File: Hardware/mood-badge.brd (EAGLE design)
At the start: 76.2 x 101.6 mm, 90 parts

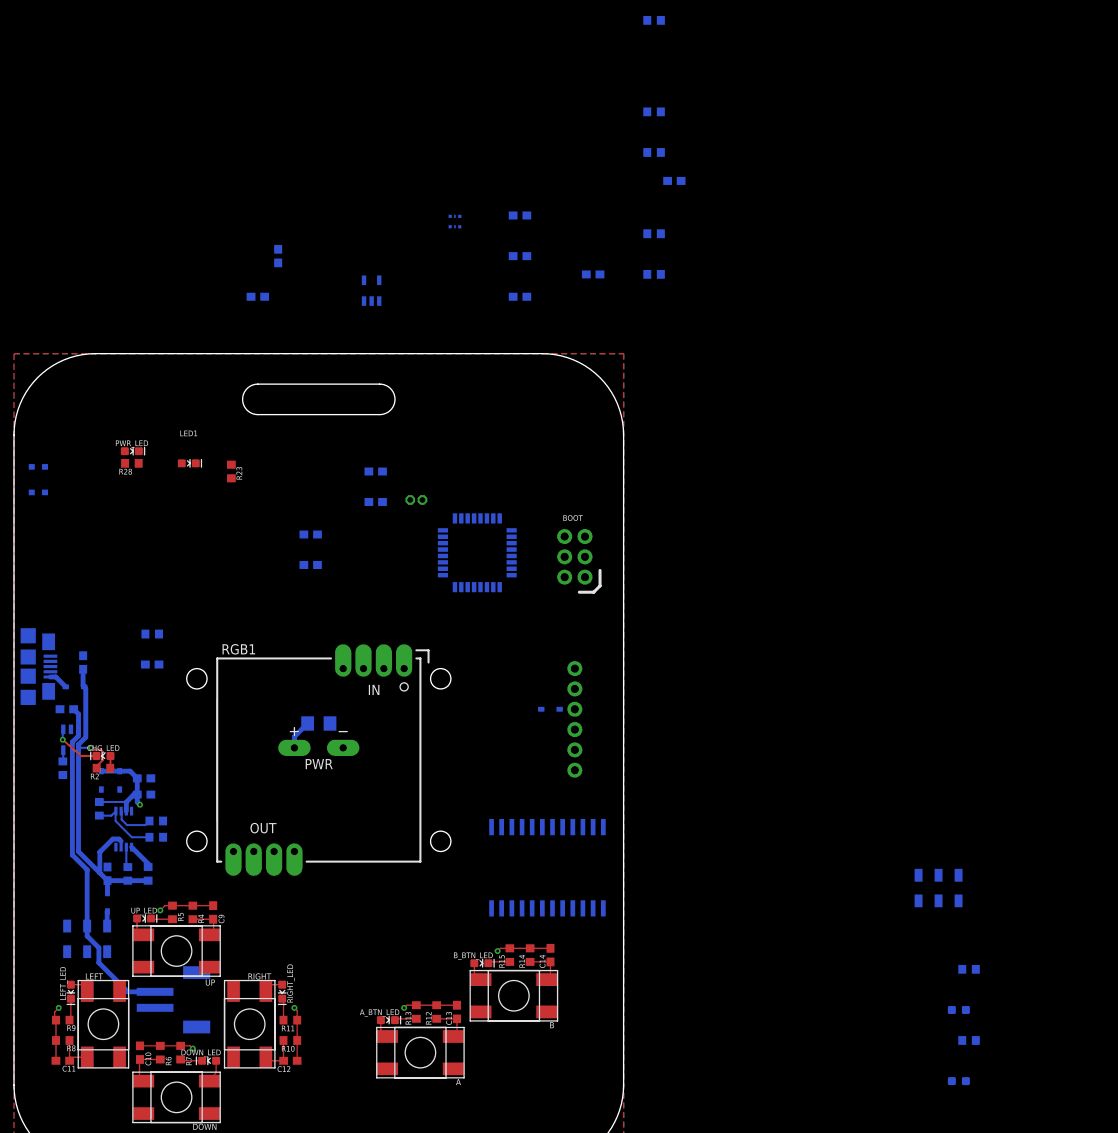
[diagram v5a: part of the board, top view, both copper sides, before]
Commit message: Adjustments to PCB trace widths and connections to buttons added
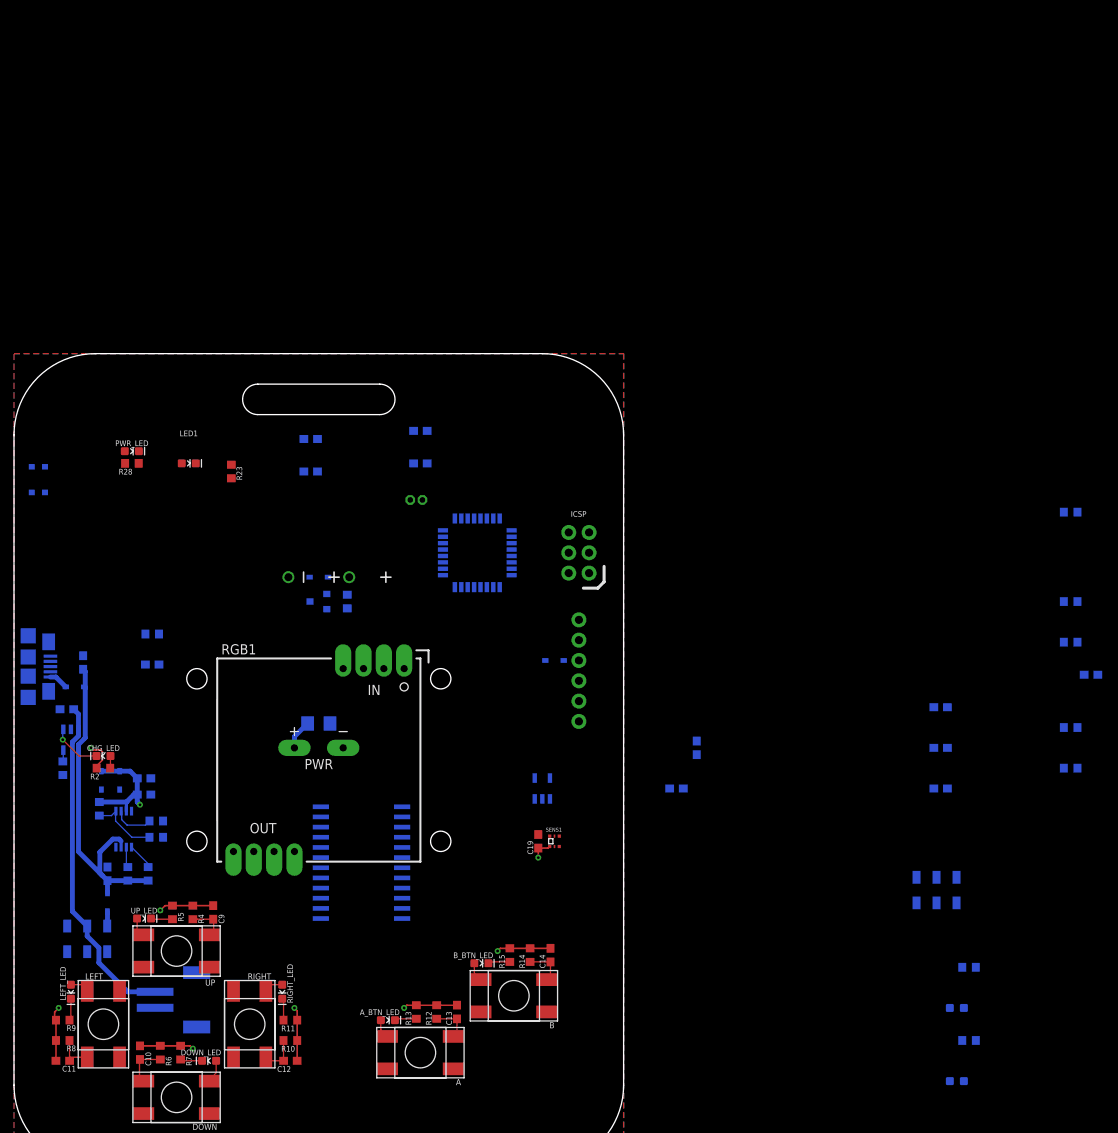
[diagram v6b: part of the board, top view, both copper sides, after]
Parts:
- removed BOOT: AVR_SPI_PROG_3X2NS, LinnesLab-Connectors:2X3-NS
- added D6: (no value), LinnesLab-DiscreteSemi:USC
- added ICSP: AVR_SPI_PROG_3X2NS, LinnesLab-Connectors:2X3-NS
- added LS1: CVS-1508, SparkFun-Electromechanical:CVS-1508_PCBSPKR
- added Q1: (no value), LinnesLab-DiscreteSemi:SOT23-3
- added R29: 180, LinnesLab-Passives:R0603
- moved C15 80.9 mm to (115.8, 57.4)
- moved C16 80.9 mm to (115.8, 52.3)
- moved C17 80.9 mm to (115.8, 47.2)
- moved R21 80.8 mm to (132.1, 54.9)
- moved R22 80.8 mm to (132.1, 49.8)
- moved C18 80.8 mm to (134.6, 61.5)
- moved C20 80.7 mm to (82.8, 47.2)
- moved C21 80.7 mm to (85.3, 52.3)
- moved R18 80.6 mm to (132.1, 81.8)
- moved R19 80.4 mm to (132.1, 70.6)
- moved R20 80.4 mm to (132.1, 65.5)
- moved SENS1 78.5 mm to (67.6, 40.6), flipped to the top
- moved C19 71.2 mm to (65.5, 40.6), flipped to the top, turned to 90 degrees
- moved OP1 65.8 mm to (66.0, 47.2)
- moved I/O 23.9 mm to (43.4, 37.3), turned to 90 degrees
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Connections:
- removed net ACTION: ARDUINO.19
- removed net LD1: ARDUINO.2
- removed net LD12: ARDUINO.14
- removed net LD13: ARDUINO.13
- removed net LD14: ARDUINO.12
- removed net LD15: ARDUINO.11
- removed net LD16: ARDUINO.10
- removed net LD2: ARDUINO.1
- removed net LD3: ARDUINO.32
- removed net LD6: ARDUINO.26
- removed net LD7: ARDUINO.25
- removed net LD8: ARDUINO.24
- removed net N$10: C10.1, DOWN.3, DOWN.4, DOWN_LED.A, R6.1
- removed net N$12: C11.1, LEFT.3, LEFT.4, LEFT_LED.A, R8.1
- removed net N$14: C12.1, R10.1, RIGHT.3, RIGHT.4, RIGHT_LED.A
- removed net N$16: A.3, A.4, A_BTN_LED.A, C13.1, R12.1
- removed net N$18: B.3, B.4, B_BTN_LED.A, C14.1, R14.1
- removed net N$8: C9.1, R4.1, UP.3, UP.4, UP_LED.A
- new net A_BTN: A.3, A.4, ARDUINO.1, A_BTN_LED.A, C13.1, R12.1
- new net B_BTN: ARDUINO.2, B.3, B.4, B_BTN_LED.A, C14.1, R14.1
- new net DOWN: ARDUINO.14, C10.1, DOWN.3, DOWN.4, DOWN_LED.A, R6.1
- new net N$31: Q1.1, R29.2
- new net N$5: D6.+, LS1.-, Q1.3
- new net SPKR: ARDUINO.12, R29.1
- new net UP: ARDUINO.13, C9.1, R4.1, UP.3, UP.4, UP_LED.A
- net GND: now also ICSP.6, Q1.2; no longer BOOT.6
- net LEFT: now also ARDUINO.11, C11.1, LEFT.3, LEFT.4, LEFT_LED.A, R8.1; no longer ARDUINO.23
- net MISO: now also ICSP.1; no longer BOOT.1
- net MOSI: now also ICSP.4; no longer BOOT.4
- net PULSE: now also ARDUINO.32
- net RESET: now also ICSP.5; no longer BOOT.5
- net RIGHT: now also ARDUINO.10, C12.1, R10.1, RIGHT.3, RIGHT.4, RIGHT_LED.A; no longer ARDUINO.22
- net SCK: now also ICSP.3; no longer BOOT.3
- net VCC: now also D6.-, ICSP.2, LS1.+; no longer BOOT.2
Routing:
- net N$10: track 10.8 -> 0.00 mm
- net DOWN: track 0.00 -> 10.8 mm
- net N$12: track 8.34 -> 0.00 mm
- net LEFT: track 0.00 -> 8.34 mm
- net UP: track 0.00 -> 7.92 mm
- net N$8: track 7.92 -> 0.00 mm
- net RIGHT: track 0.00 -> 7.51 mm
- net N$14: track 7.51 -> 0.00 mm
- net N$16: track 7.32 -> 0.00 mm
- net A_BTN: track 0.00 -> 7.32 mm
- net N$18: track 7.32 -> 0.00 mm
- net B_BTN: track 0.00 -> 7.32 mm
- net GND: track 41.6 -> 44.4 mm, vias 6 -> 7
- net VIN: track 47.2 -> 46.2 mm
- net V_USB: track 2.43 -> 3.10 mm

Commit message: PCB Routed
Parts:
- removed CHG_LED, PWR_LED: (no value), LinnesLab-LED:LED-0603
- removed I/O: PCF8575C, SparkFun-Retired:SO-24DW
- added CHG, PWR: (no value), LinnesLab-LED:LED-0603
- moved MODE_2 86.1 mm to (61.5, 75.7), flipped to the top, turned to 180 degrees
- moved R17 84.8 mm to (61.5, 77.7), flipped to the top
- moved MODE_1 83.8 mm to (61.5, 81.8), flipped to the top
- moved R16 79.8 mm to (61.5, 79.8), flipped to the top, turned to 180 degrees
- moved R19 70.7 mm to (62.5, 58.4), turned to 270 degrees
- moved R21 69.6 mm to (62.5, 53.8), turned to 90 degrees
- moved R18 69.4 mm to (68.6, 53.8), turned to 90 degrees
- moved R22 68.2 mm to (64.0, 53.8), turned to 270 degrees
- moved C18 67.0 mm to (68.6, 50.3), turned to 90 degrees
- moved R20 66.2 mm to (68.6, 46.7), turned to 90 degrees
- moved MODE 66.2 mm to (66.0, 78.7), flipped to the top, turned to 90 degrees
- moved RESET 62.7 mm to (65.5, 91.4), turned to 0 degrees
- moved LED1 61.1 mm to (67.1, 46.7), turned to 90 degrees
- moved R23 57.8 mm to (68.8, 46.7)
- moved C15 49.9 mm to (67.1, 46.7), turned to 90 degrees
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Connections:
- removed net N$22: MODE_1.C, R16.1
- new net N$8: MODE_1.A, R16.2
- net A_BTN: now also ARDUINO.10; no longer ARDUINO.1
- net B_BTN: now also ARDUINO.9; no longer ARDUINO.2
- net DOWN: now also ARDUINO.12; no longer ARDUINO.14
- net GND: now also MODE_1.C; no longer I/O.12, I/O.2, I/O.21, I/O.3, R16.2
- net LEFT: now also ARDUINO.13; no longer ARDUINO.11
- net MODE: now also ARDUINO.2, R16.1; no longer ARDUINO.9, MODE_1.A
- net N$3: now also CHG.A; no longer CHG_LED.A
- net N$32: now also PWR.C; no longer PWR_LED.C
- net RIGHT: now also ARDUINO.11; no longer ARDUINO.10
- net SCL: no longer I/O.22
- net SDA: no longer I/O.23
- net SPKR: now also ARDUINO.1; no longer ARDUINO.12
- net STAT: now also CHG.C; no longer CHG_LED.C
- net UP: now also ARDUINO.14; no longer ARDUINO.13
- net VCC: now also PWR.A; no longer I/O.24, PWR_LED.A
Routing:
- net LEFT: track 8.34 -> 96.9 mm, vias 0 -> 1
- net DOWN: track 10.8 -> 85.1 mm, vias 0 -> 1
- net B_BTN: track 7.32 -> 78.3 mm, vias 0 -> 1
- net A_BTN: track 7.32 -> 75.8 mm, vias 0 -> 1
- net RIGHT: track 7.51 -> 67.6 mm, vias 0 -> 1
- net UP: track 7.92 -> 66.7 mm, vias 0 -> 1
- net RESET: track 0.00 -> 48.0 mm, vias 0 -> 1
- net SCK: track 0.00 -> 30.8 mm, vias 0 -> 1
- net MOSI: track 0.00 -> 30.0 mm, vias 0 -> 1
- net PULSE: track 0.00 -> 30.0 mm
- net MISO: track 0.00 -> 22.1 mm, vias 0 -> 1
- net VCC: track 18.5 -> 38.6 mm, vias 1 -> 6
- net SPKR: track 0.00 -> 16.6 mm
- net MODE: track 0.00 -> 12.4 mm, vias 0 -> 1
- net GND: track 44.4 -> 55.7 mm, vias 7 -> 10
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
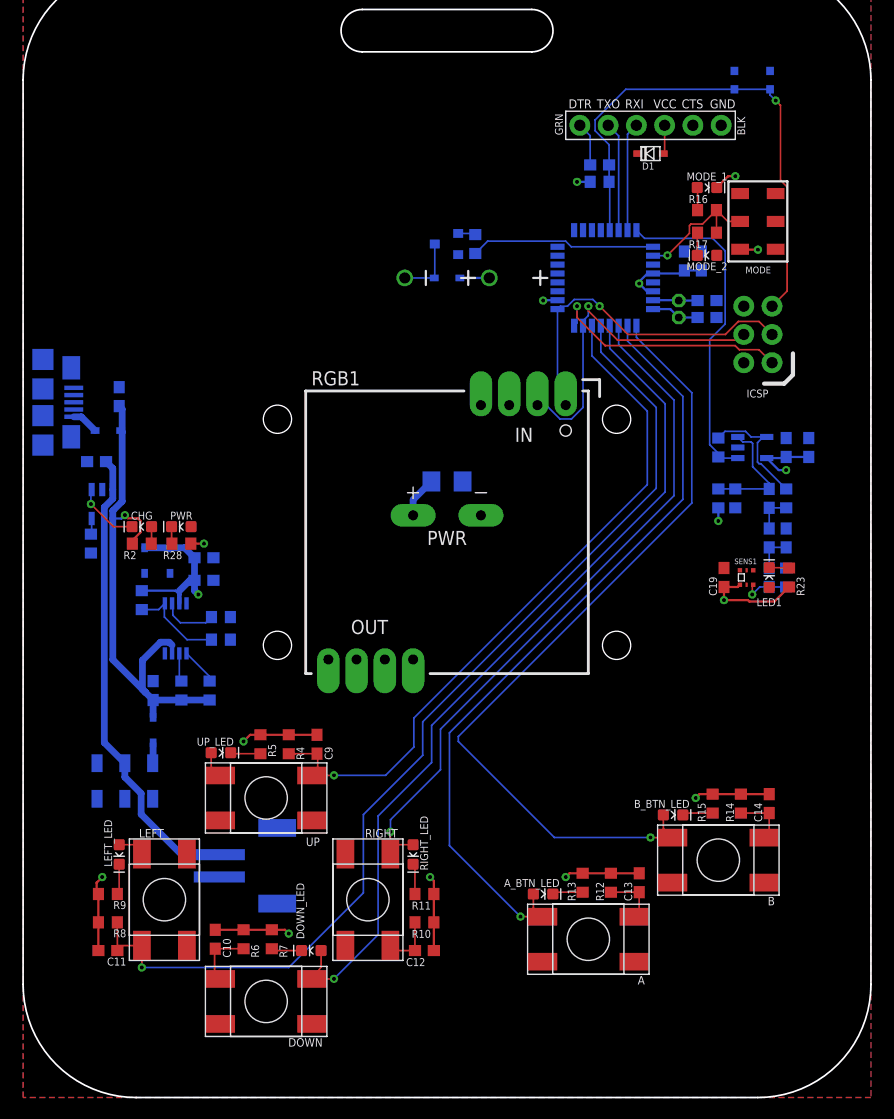
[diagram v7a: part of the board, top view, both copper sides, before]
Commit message: Swap out matrix for different part with better connector layout
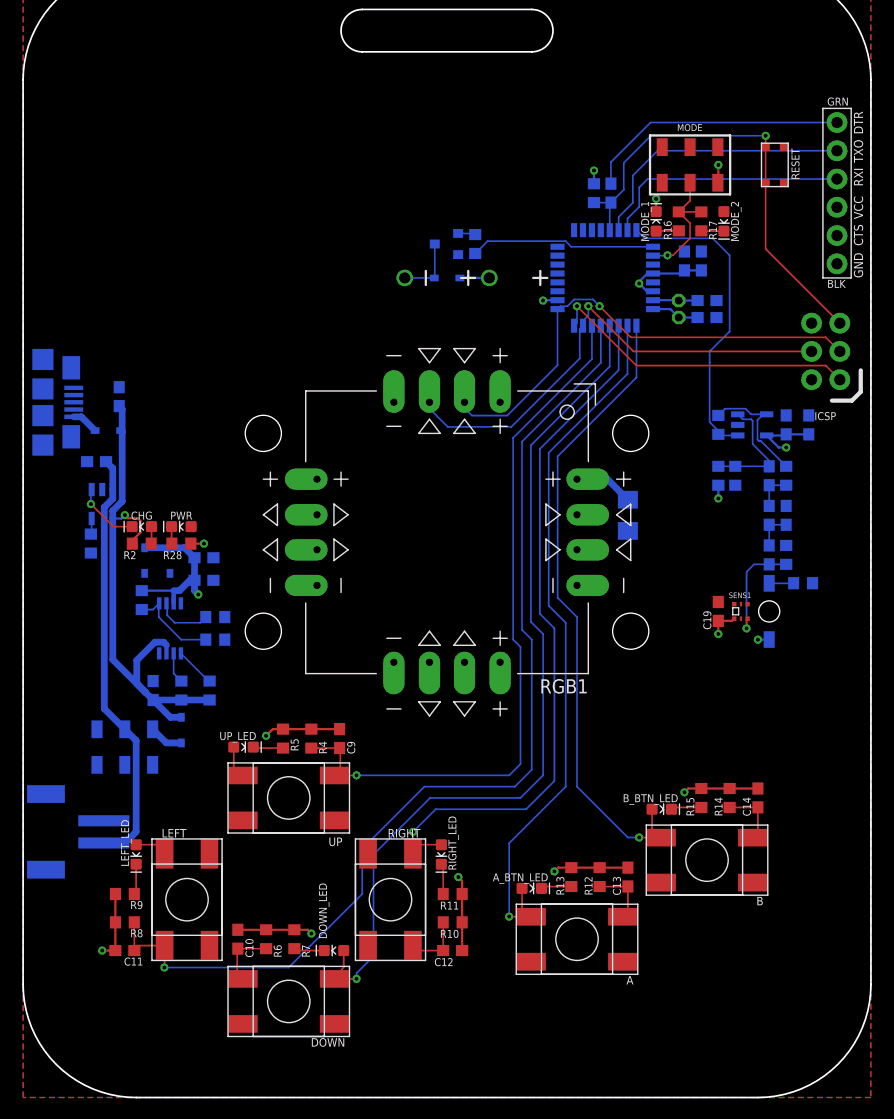
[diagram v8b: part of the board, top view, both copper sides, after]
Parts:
- removed D1: (no value), LinnesLab-DiscreteSemi:USC
- LED1: device LinnesLab-LED:LED-0603 -> LinnesLab-LED:2-SMD.Z-BEND
- RGB1: value (none) -> SPARKFUN_LUMINI_8X8_COM-15247; device mood-badge-components:ADA_DOTSTAR_8X8_3444_HOLES -> mood-badge-components:SPARKFUN_LUMINI_8X8_COM-15047
- moved LIPO 18.0 mm to (3.56, 23.9), turned to 270 degrees
- moved RGB1 18.0 mm to (38.1, 50.8), turned to 180 degrees
- moved FTDI 17.8 mm to (73.2, 81.3), turned to 270 degrees
- moved C6 16.5 mm to (54.4, 52.3), turned to 270 degrees
- moved MODE 7.94 mm to (59.9, 83.8), turned to 180 degrees
- moved RESET 7.89 mm to (67.6, 83.8), flipped to the top, turned to 270 degrees
- moved ICSP 6.28 mm to (72.1, 67.1)
- moved MODE_1 5.49 mm to (56.9, 78.7), turned to 90 degrees
- moved MODE_2 3.41 mm to (63.0, 78.7), turned to 270 degrees
- moved C19 3.09 mm to (62.5, 43.7)
- moved SENS1 3.09 mm to (64.5, 43.7)
- moved POWER 3.05 mm to (9.14, 31.5)
- moved LED1 3.05 mm to (67.1, 43.7), flipped to the bottom
- moved R16 2.74 mm to (58.9, 78.7), turned to 270 degrees
- moved C5 2.74 mm to (52.8, 81.3), turned to 270 degrees
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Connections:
- removed net N$6: D1.+, FTDI.VCC
- net GND: now also RGB1.GND_0, RGB1.GND_1, RGB1.GND_2, RGB1.GND_3; no longer RGB1.GND, RGB1.GND_IN, RGB1.GND_OUT
- net MOSI: now also RGB1.DI_0, RGB1.DI_1; no longer RGB1.DIN
- net N$28: now also LED1.-; no longer LED1.C
- net SCK: now also RGB1.CI_0, RGB1.CI_1; no longer RGB1.CIN
- net VCC: now also FTDI.VCC, LED1.+, RGB1.5V_0, RGB1.5V_1, RGB1.5V_2, RGB1.5V_3; no longer D1.-, LED1.A, RGB1.VDD, RGB1.VDD_IN, RGB1.VDD_OUT
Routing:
- net DTR: track 3.94 -> 23.7 mm
- net B_BTN: track 78.3 -> 62.9 mm
- net RXD: track 9.82 -> 24.7 mm
- net MOSI: track 30.0 -> 44.1 mm
- net SCK: track 30.8 -> 43.7 mm
- net TXD: track 9.75 -> 22.4 mm
- net GND: track 55.7 -> 47.7 mm
- net A_BTN: track 75.8 -> 69.1 mm
- net RESET: track 48.0 -> 41.5 mm
- net MISO: track 22.1 -> 28.2 mm
- net N$20: track 4.24 -> 9.83 mm
- net VLIPO: track 42.2 -> 38.3 mm
- net N$6: track 2.59 -> 0.00 mm
- net VCC: track 38.6 -> 41.1 mm, vias 6 -> 7
- net UP: track 66.7 -> 68.7 mm
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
